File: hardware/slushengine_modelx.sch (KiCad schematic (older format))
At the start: 76 parts, among them J1001 UEXT1, P1 CONN_01X03, P1001 CONN_01X02, P1002 CONN_01X02, P1003 Raspberry_Pi_+_Conn, P1004 CONN_01X06, P1005 CONN_01X08, P1006 CONN_01X08, P1007 TST, P1008 TST, P1009 TST, P1010 TST, P1011 TST, P1012 TST, P1013 TST, P1014 TST, P1015 TST, P1016 TST, P1017 TST, P1018 TST, P1019 TST, P1020 TST, P1021 TST, P1022 TST, P1023 TST, P1024 TST, P1025 TST, P1026 TST, P1027 TST, P1028 TST, P1029 TST, P1030 TST, P1031 TST, P1032 CONN_01X06, P1033 CONN_01X06, P1034 CONN_01X06, P1036 CONN_01X02, U1001 CAT24C32HU4I-GT3, U1002 LM3489, U1003 FDC5614P, U1004 LM1117IMPX-ADJ, U1005 MCP23017, U1006 MAX1164x

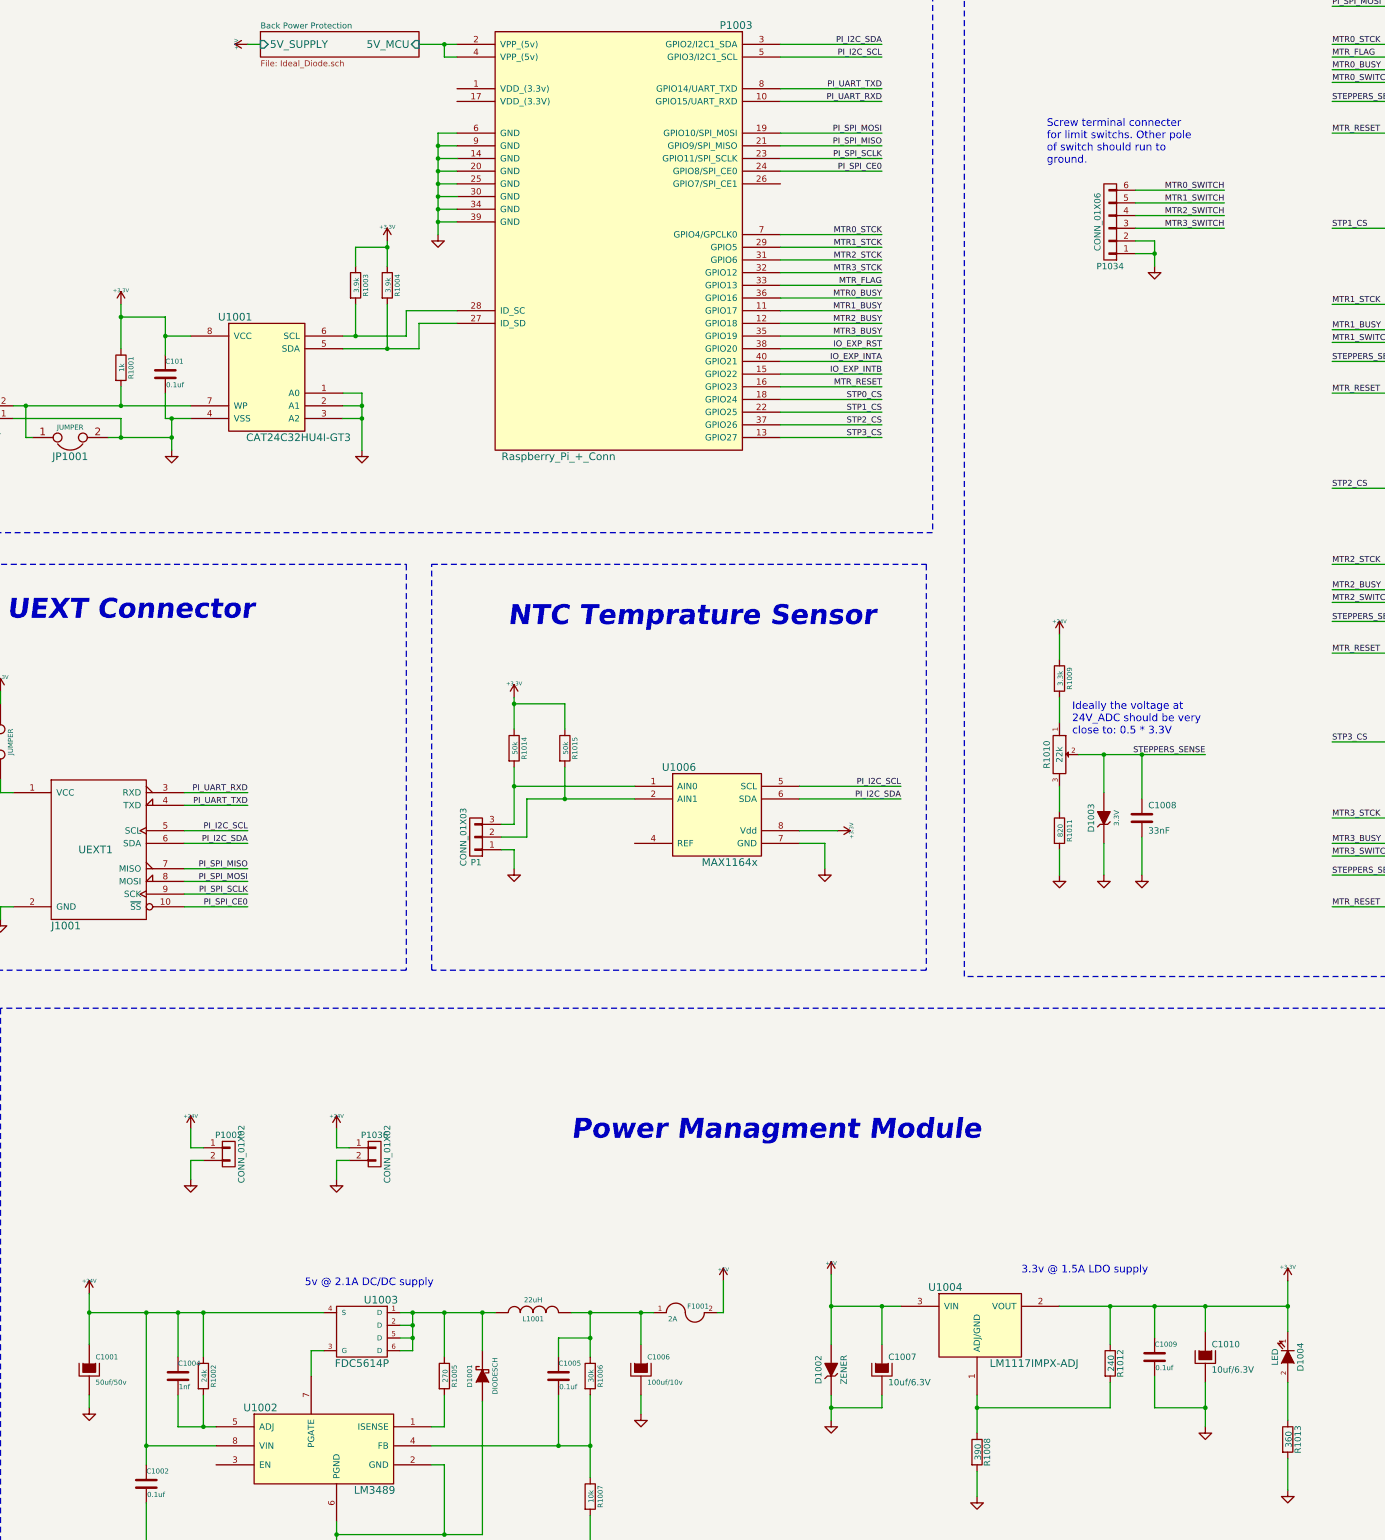
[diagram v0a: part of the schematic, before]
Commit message: added some new part numbers
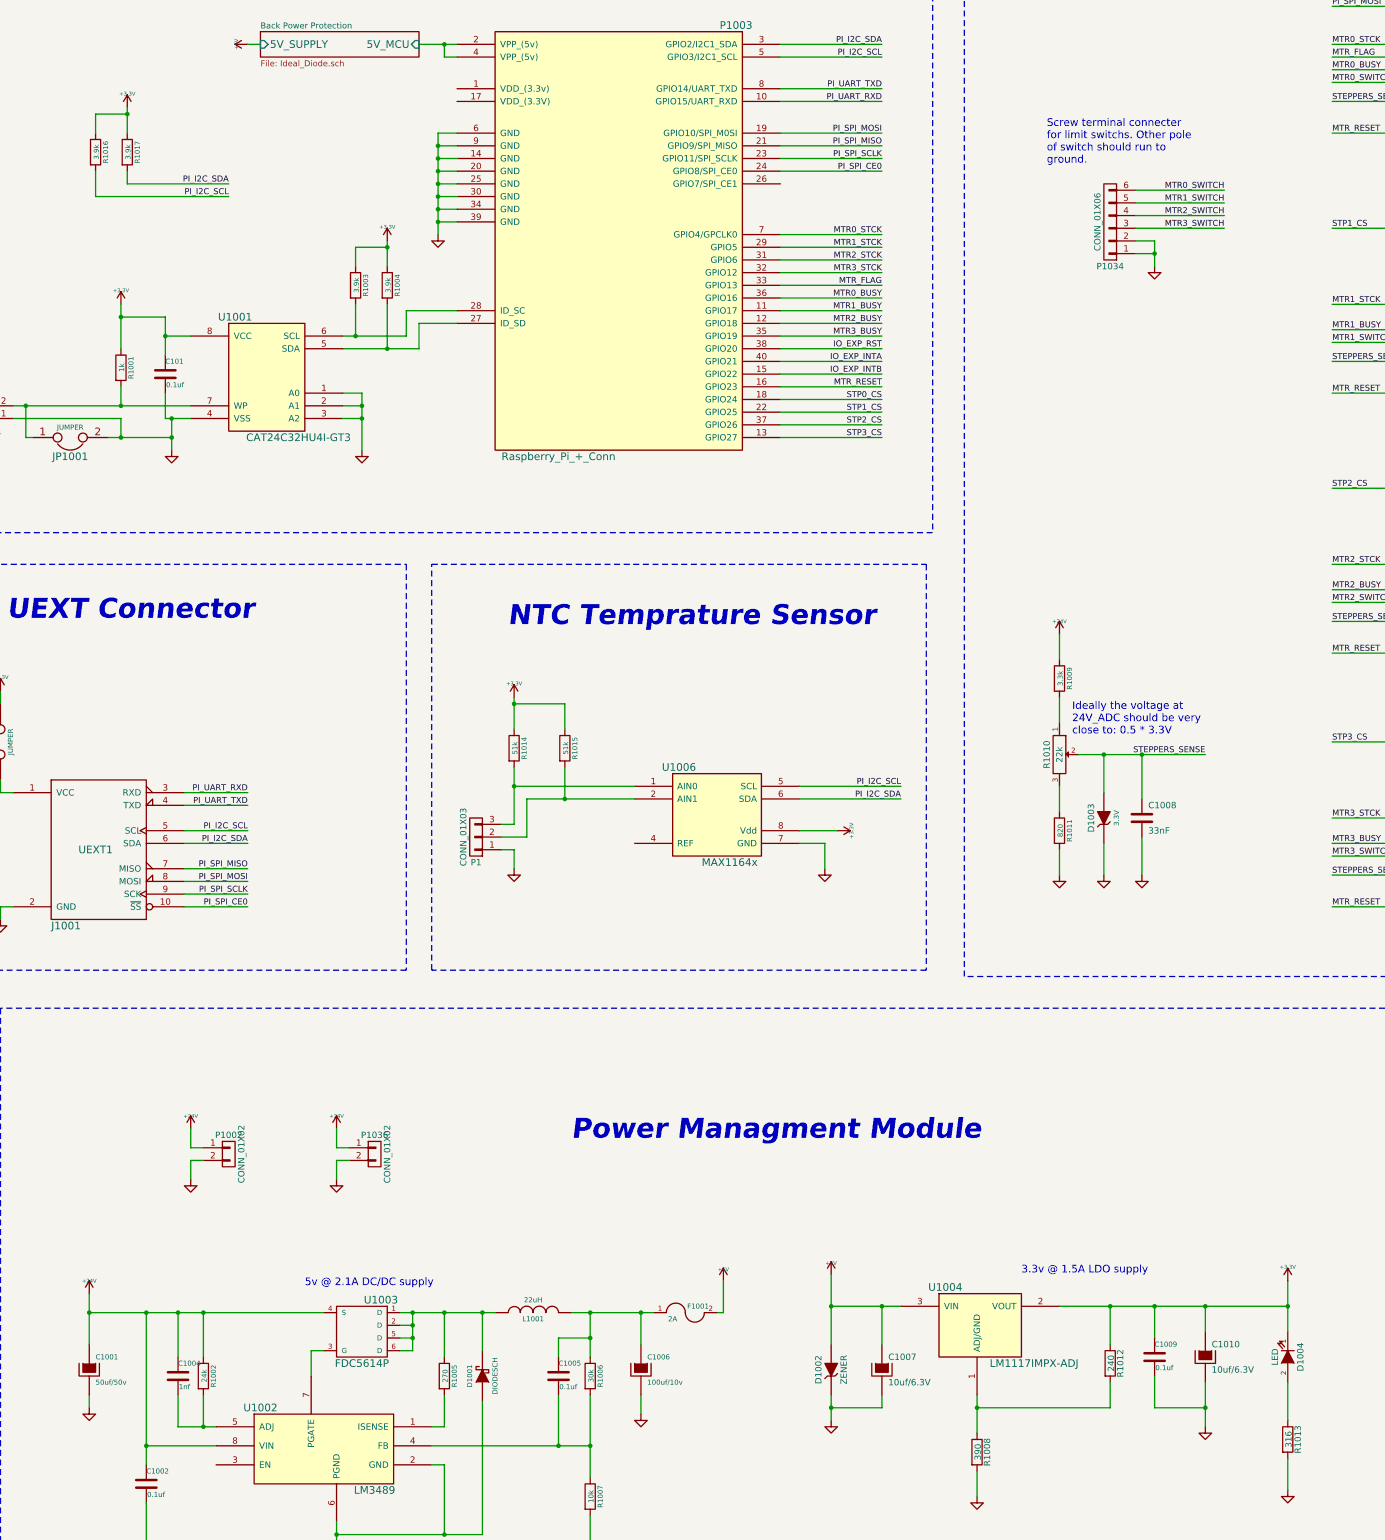
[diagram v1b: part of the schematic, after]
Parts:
- added R1016, R1017: 3.9k, w_smd_resistors:r_0402, symbol R
- C1004: Mouser Part No. 810-C1005C0G2A102J5C -> 810-C1005X5R1H102K
- D1004: Mouser Part No. 743-HT-191USD -> 720-LSQ976-NR-1
- R1005: Mouser Part No. 667-ERJ-P6WJ271V -> 667-ERJ-P06J271V
- R1013: value 360 -> 316; Mouser Part No. 71-CRCW0603316RFKEB -> 667-ERJ-2RKF3160X
- R1014, R1015: value 50k -> 51k; Mouser Part No. 71-CRCW0402-50K-E3 -> 754-RR0510P-513D
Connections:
- net +3V3: now also R1016.1, R1017.1
- net PI_I2C_SCL: now also R1016.2
- net PI_I2C_SDA: now also R1017.2
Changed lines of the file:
@@
 EESchema Schematic File Version 2
-LIBS:power
-LIBS:device
-LIBS:transistors
-LIBS:conn
-LIBS:linear
-LIBS:regul
-LIBS:74xx
-LIBS:cmos4000
-LIBS:adc-dac
-LIBS:memory
-LIBS:xilinx
-LIBS:special
-LIBS:microcontrollers
-LIBS:dsp
-LIBS:microchip
-LIBS:analog_switches
-LIBS:motorola
-LIBS:texas
-LIBS:intel
-LIBS:audio
-LIBS:interface
-LIBS:digital-audio
-LIBS:philips
-LIBS:display
-LIBS:cypress
-LIBS:siliconi
-LIBS:opto
-LIBS:atmel
-LIBS:contrib
-LIBS:valves
 LIBS:cat24c32hu4i-gt3
 LIBS:components
@@
 LIBS:raspberry_pi_+_conn
 LIBS:max1164x
-LIBS:motion_engine_hatish-cache
+LIBS:slushengine_modelx-cache
 EELAYER 25 0
 EELAYER END
@@
 F 2 "w_smd_cap:c_0402" H 2738 12850 30  0001 C CNN
 F 3 "" H 2700 13000 60  0000 C CNN
-F 4 "810-C1005C0G2A102J5C" H 2700 13000 60  0001 C CNN "Mouser Part No."
+F 4 "810-C1005X5R1H102K" H 2700 13000 60  0001 C CNN "Mouser Part No."
 	1    2700 13000
 	1    0    0    -1
@@
 F 2 "w_smd_resistors:r_0805" V 4730 13000 30  0001 C CNN
 F 3 "" H 4800 13000 30  0000 C CNN
-F 4 "667-ERJ-P6WJ271V" V 4800 13000 60  0001 C CNN "Mouser Part No."
+F 4 "667-ERJ-P06J271V" V 4800 13000 60  0001 C CNN "Mouser Part No."
 	1    4800 13000
 	1    0    0    -1
@@
 F 2 "w_smd_leds:Led_0603" H 11450 12850 60  0001 C CNN
 F 3 "" H 11450 12850 60  0000 C CNN
-F 4 "743-HT-191USD" H 11450 12850 60  0001 C CNN "Mouser Part No."
+F 4 "720-LSQ976-NR-1" H 11450 12850 60  0001 C CNN "Mouser Part No."
 	1    11450 12850
 	0    1    1    0
@@
 P 11450 13500
 F 0 "R1013" V 11530 13500 50  0000 C CNN
-F 1 "360" V 11457 13501 50  0000 C CNN
+F 1 "316" V 11457 13501 50  0000 C CNN
 F 2 "w_smd_resistors:r_0402" V 11380 13500 30  0001 C CNN
 F 3 "" H 11450 13500 30  0000 C CNN
-F 4 "71-CRCW0603316RFKEB" V 11450 13500 60  0001 C CNN "Mouser Part No."
+F 4 "667-ERJ-2RKF3160X " V 11450 13500 60  0001 C CNN "Mouser Part No."
 	1    11450 13500
 	1    0    0    -1
@@
 P 5750 8050
 F 0 "R1015" V 5830 8050 40  0000 C CNN
-F 1 "50k" V 5757 8051 40  0000 C CNN
+F 1 "51k" V 5757 8051 40  0000 C CNN
 F 2 "w_smd_resistors:r_0402" V 5680 8050 30  0001 C CNN
 F 3 "http://www.digikey.ca/product-detail/en/MCR50JZHJ332/RHM3.3KBGCT-ND/2291227" H 5750 8050 30  0001 C CNN
 F 4 "71-CRCW0402-50K-E3" H 900 -7300 60  0001 C CNN "Digikey Number"
-F 5 "71-CRCW0402-50K-E3" V 5750 8050 60  0001 C CNN "Mouser Part No."
+F 5 "754-RR0510P-513D" V 5750 8050 60  0001 C CNN "Mouser Part No."
 	1    5750 8050
 	1    0    0    -1
@@
 P 5350 8050
 F 0 "R1014" V 5430 8050 40  0000 C CNN
-F 1 "50k" V 5357 8051 40  0000 C CNN
+F 1 "51k" V 5357 8051 40  0000 C CNN
 F 2 "w_smd_resistors:r_0402" V 5280 8050 30  0001 C CNN
 F 3 "http://www.digikey.ca/product-detail/en/MCR50JZHJ332/RHM3.3KBGCT-ND/2291227" H 5350 8050 30  0001 C CNN
 F 4 "71-CRCW0402-50K-E3" H 500 -7300 60  0001 C CNN "Digikey Number"
-F 5 "71-CRCW0402-50K-E3" V 5350 8050 60  0001 C CNN "Mouser Part No."
+F 5 "754-RR0510P-513D" V 5350 8050 60  0001 C CNN "Mouser Part No."
 	1    5350 8050
 	1    0    0    -1
@@
 Wire Wire Line
 	5350 8850 5350 9000
+$Comp
+L R R1016
+U 1 1 55802103
+P 2050 3350
+F 0 "R1016" V 2130 3350 40  0000 C CNN
+F 1 "3.9k" V 2057 3351 40  0000 C CNN
+F 2 "w_smd_resistors:r_0402" V 1980 3350 30  0001 C CNN
+F 3 "" H 2050 3350 30  0000 C CNN
+F 4 "71-CRCW04023K90FKED" V 2050 3350 60  0001 C CNN "Mouser Part No."
+	1    2050 3350
+	1    0    0    -1
+$EndComp
+$Comp
+L R R1017
+U 1 1 5580210A
+P 2300 3350
+F 0 "R1017" V 2380 3350 40  0000 C CNN
+F 1 "3.9k" V 2307 3351 40  0000 C CNN
+F 2 "w_smd_resistors:r_0402" V 2230 3350 30  0001 C CNN
+F 3 "" H 2300 3350 30  0000 C CNN
+F 4 "71-CRCW04023K90FKED" V 2300 3350 60  0001 C CNN "Mouser Part No."
+	1    2300 3350
+	1    0    0    -1
+$EndComp
+$Comp
+L +3.3V #PWR048
+U 1 1 55802110
+P 2300 3000
+F 0 "#PWR048" H 2300 2960 30  0001 C CNN
+F 1 "+3.3V" H 2300 3110 30  0000 C CNN
+F 2 "" H 2300 3000 60  0000 C CNN
+F 3 "" H 2300 3000 60  0000 C CNN
+	1    2300 3000
+	1    0    0    -1
+$EndComp
+Connection ~ 2300 3050
+Wire Wire Line
+	2050 3050 2050 3200
+Wire Wire Line
+	2300 3050 2050 3050
+Wire Wire Line
+	2300 3000 2300 3200
+Text Label 3100 3700 2    47   ~ 0
+PI_I2C_SCL
+Text Label 3100 3600 2    47   ~ 0
+PI_I2C_SDA
+Wire Wire Line
+	2050 3700 3100 3700
+Wire Wire Line
+	2300 3600 3100 3600
+Wire Wire Line
+	2300 3500 2300 3600
+Wire Wire Line
+	2050 3700 2050 3500
 $EndSCHEMATC

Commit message: small board changes
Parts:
- renumbered P1 to P1035
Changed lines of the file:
@@
 $EndComp
 $Comp
-L CONN_01X03 P1
+L CONN_01X03 P1035
 U 1 1 5579BE23
 P 5050 8750
-F 0 "P1" H 5050 8950 50  0000 C CNN
-F 1 "CONN_01X03" V 5150 8750 50  0000 C CNN
+F 0 "P1035" H 5050 8950 50  0000 C CNN
+F 1 "CONN_01X03" V 5150 8750 50  0001 C CNN
 F 2 "w_conn_mkds:mkds_1,5-3" H 5050 8750 60  0001 C CNN
 F 3 "" H 5050 8750 60  0000 C CNN
